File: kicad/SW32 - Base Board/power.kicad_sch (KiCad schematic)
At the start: 35 parts, among them J23 PWR, J24 BAT, SW1 PWR, U5 LM2941, U6 TPS5430DDA, U7 NCP1117LP

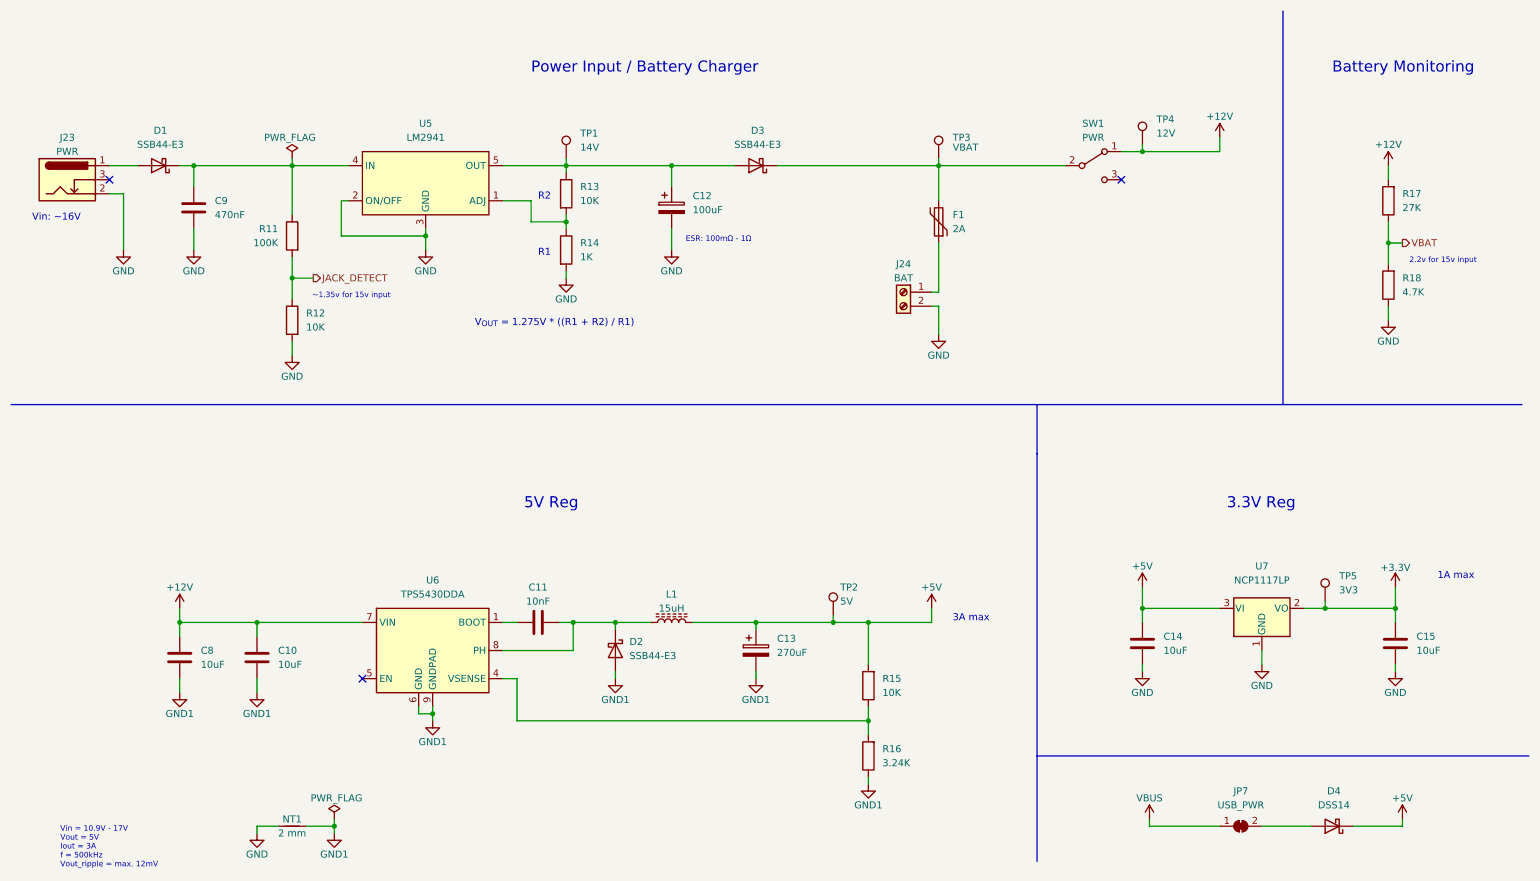
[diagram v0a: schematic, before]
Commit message: use ESP32
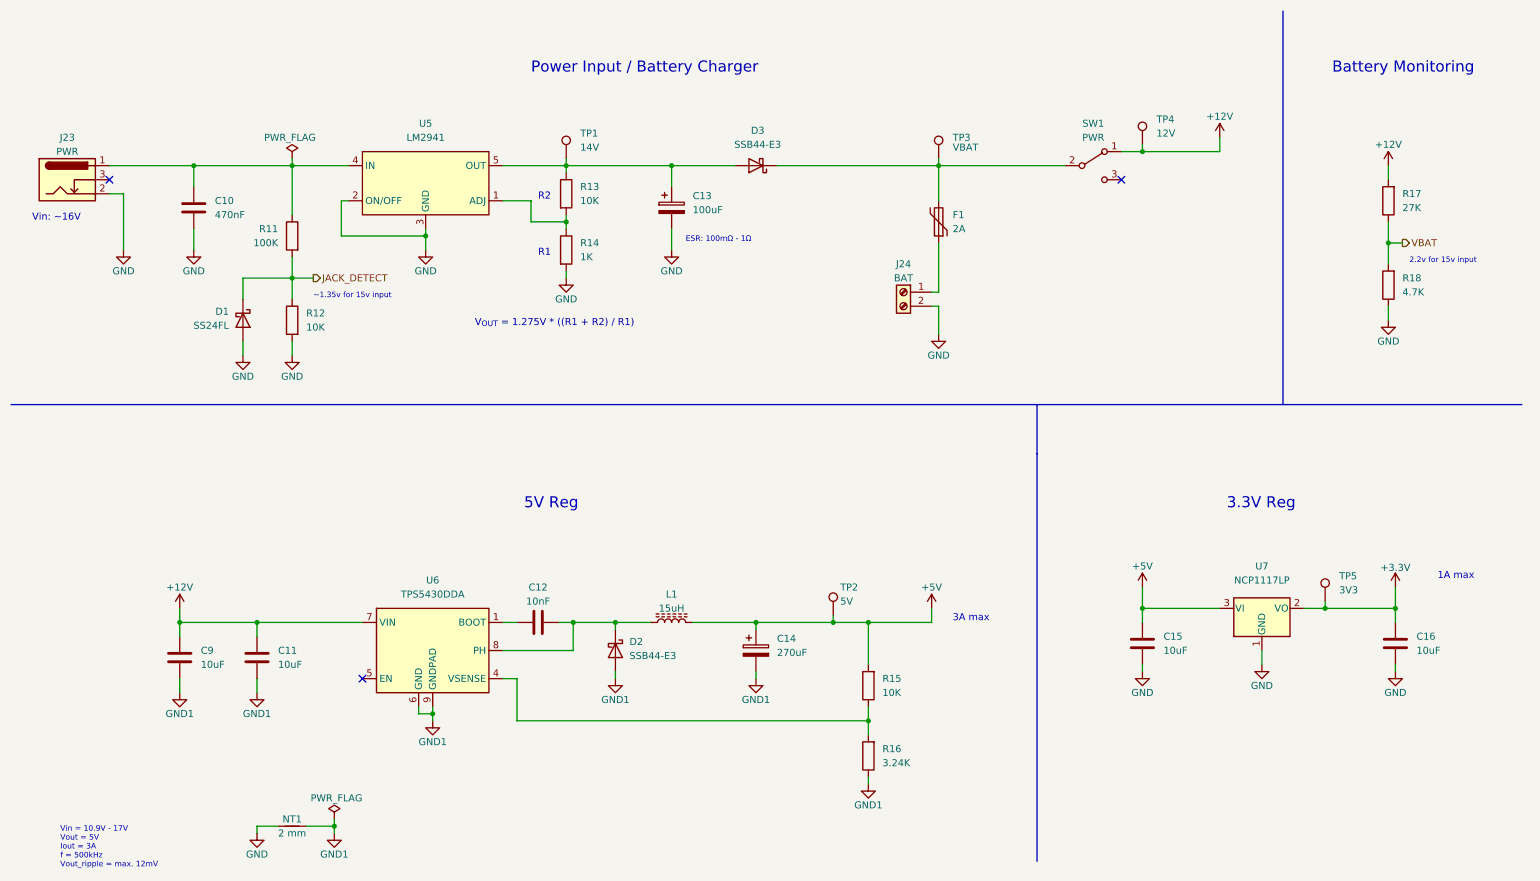
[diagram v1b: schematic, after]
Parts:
- removed D4: DSS14, Diode_SMD:D_SOD-123F, symbol Device:D_Schottky
- removed JP7: USB_PWR, Jumper:SolderJumper-2_P1.3mm_Bridged_RoundedPad1.0x1.5mm, symbol Jumper:SolderJumper_2_Bridged
- D1: value SSB44-E3 -> SS24FL; footprint Diode_SMD:D_SMB -> Diode_SMD:D_SOD-123F; LCSC C466999 -> C894433; MOUSER 625-SSB44-E3 -> 512-SS24FL; MPN SSB44-E3/52T -> SS24FL
- renumbered C9 to C10, C10 to C11, C11 to C12, C12 to C13, C13 to C14, C14 to C15, C15 to C16, C8 to C9
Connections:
- net GND: now also D1.2 (A)
- net JACK_DETECT: now also D1.1 (K)
- net at C10.1, R11.1, U5.4 (IN): now also J23.1; no longer D1.1 (K)
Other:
- moved on the sheet: D1

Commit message: add cap
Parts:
- renumbered C9 to C10, C10 to C11, C11 to C12, C12 to C13, C13 to C14, C14 to C15, C15 to C16, C16 to C17
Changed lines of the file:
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@@
   (symbol (lib_id "Device:C") (at 215.9 127 0) (unit 1)
     (in_bom yes) (on_board yes) (fields_autoplaced)
-    (property "Reference" "C15" (id 0) (at 219.71 125.7299 0)
+    (property "Reference" "C16" (id 0) (at 219.71 125.7299 0)
       (effects (font (size 1.27 1.27)) (justify left))
     )
@@
   (symbol (lib_id "power:GND1") (at 87.63 140.97 0) (unit 1)
     (in_bom yes) (on_board yes)
-    (property "Reference" "#PWR068" (id 0) (at 87.63 147.32 0)
+    (property "Reference" "#PWR070" (id 0) (at 87.63 147.32 0)
       (effects (font (size 1.27 1.27)) hide)
     )
@@
   (symbol (lib_id "power:GND") (at 53.34 74.93 0) (mirror y) (unit 1)
     (in_bom yes) (on_board yes)
-    (property "Reference" "#PWR062" (id 0) (at 53.34 81.28 0)
+    (property "Reference" "#PWR064" (id 0) (at 53.34 81.28 0)
       (effects (font (size 1.27 1.27)) hide)
     )
@@
   (symbol (lib_id "power:+12V") (at 41.91 120.65 0) (unit 1)
     (in_bom yes) (on_board yes)
-    (property "Reference" "#PWR059" (id 0) (at 41.91 124.46 0)
+    (property "Reference" "#PWR061" (id 0) (at 41.91 124.46 0)
       (effects (font (size 1.27 1.27)) hide)
     )
@@
   (symbol (lib_id "power:GND") (at 86.36 55.88 0) (unit 1)
     (in_bom yes) (on_board yes)
-    (property "Reference" "#PWR067" (id 0) (at 86.36 62.23 0)
+    (property "Reference" "#PWR069" (id 0) (at 86.36 62.23 0)
       (effects (font (size 1.27 1.27)) hide)
     )
@@
   (symbol (lib_id "Device:C") (at 106.68 123.19 90) (unit 1)
     (in_bom yes) (on_board yes)
-    (property "Reference" "C12" (id 0) (at 106.68 116.84 90))
+    (property "Reference" "C13" (id 0) (at 106.68 116.84 90))
     (property "Value" "10nF" (id 1) (at 106.68 119.38 90))
     (property "Footprint" "Capacitor_SMD:C_0603_1608Metric" (id 2) (at 110.49 122.2248 0)
@@
   (symbol (lib_id "power:+12V") (at 229.87 35.56 0) (unit 1)
     (in_bom yes) (on_board yes)
-    (property "Reference" "#PWR078" (id 0) (at 229.87 39.37 0)
+    (property "Reference" "#PWR080" (id 0) (at 229.87 39.37 0)
       (effects (font (size 1.27 1.27)) hide)
     )
@@
   (symbol (lib_id "power:GND") (at 111.76 60.96 0) (unit 1)
     (in_bom yes) (on_board yes)
-    (property "Reference" "#PWR069" (id 0) (at 111.76 67.31 0)
+    (property "Reference" "#PWR071" (id 0) (at 111.76 67.31 0)
       (effects (font (size 1.27 1.27)) hide)
     )
@@
   (symbol (lib_id "power:GND") (at 260.35 68.58 0) (unit 1)
     (in_bom yes) (on_board yes)
-    (property "Reference" "#PWR081" (id 0) (at 260.35 74.93 0)
+    (property "Reference" "#PWR083" (id 0) (at 260.35 74.93 0)
       (effects (font (size 1.27 1.27)) hide)
     )
@@
   (symbol (lib_id "power:GND") (at 62.23 74.93 0) (mirror y) (unit 1)
     (in_bom yes) (on_board yes)
-    (property "Reference" "#PWR065" (id 0) (at 62.23 81.28 0)
+    (property "Reference" "#PWR067" (id 0) (at 62.23 81.28 0)
       (effects (font (size 1.27 1.27)) hide)
     )
@@
   (symbol (lib_id "power:+5V") (at 215.9 116.84 0) (unit 1)
     (in_bom yes) (on_board yes)
-    (property "Reference" "#PWR076" (id 0) (at 215.9 120.65 0)
+    (property "Reference" "#PWR078" (id 0) (at 215.9 120.65 0)
       (effects (font (size 1.27 1.27)) hide)
     )
@@
   (symbol (lib_id "power:GND1") (at 69.85 161.29 0) (mirror y) (unit 1)
     (in_bom yes) (on_board yes)
-    (property "Reference" "#PWR066" (id 0) (at 69.85 167.64 0)
+    (property "Reference" "#PWR068" (id 0) (at 69.85 167.64 0)
       (effects (font (size 1.27 1.27)) hide)
     )
@@
   (symbol (lib_id "power:GND") (at 44.45 55.88 0) (unit 1)
     (in_bom yes) (on_board yes)
-    (property "Reference" "#PWR061" (id 0) (at 44.45 62.23 0)
+    (property "Reference" "#PWR063" (id 0) (at 44.45 62.23 0)
       (effects (font (size 1.27 1.27)) hide)
     )
@@
   (symbol (lib_id "power:GND") (at 130.81 55.88 0) (unit 1)
     (in_bom yes) (on_board yes)
-    (property "Reference" "#PWR071" (id 0) (at 130.81 62.23 0)
+    (property "Reference" "#PWR073" (id 0) (at 130.81 62.23 0)
       (effects (font (size 1.27 1.27)) hide)
     )
@@
   (symbol (lib_id "power:GND") (at 179.07 71.12 0) (unit 1)
     (in_bom yes) (on_board yes)
-    (property "Reference" "#PWR075" (id 0) (at 179.07 77.47 0)
+    (property "Reference" "#PWR077" (id 0) (at 179.07 77.47 0)
       (effects (font (size 1.27 1.27)) hide)
     )
@@
   (symbol (lib_id "Device:C") (at 44.45 48.26 0) (unit 1)
     (in_bom yes) (on_board yes) (fields_autoplaced)
-    (property "Reference" "C10" (id 0) (at 48.26 46.9899 0)
+    (property "Reference" "C11" (id 0) (at 48.26 46.9899 0)
       (effects (font (size 1.27 1.27)) (justify left))
     )
@@
   (symbol (lib_id "Device:C_Polarized") (at 146.05 128.27 0) (unit 1)
     (in_bom yes) (on_board yes) (fields_autoplaced)
-    (property "Reference" "C14" (id 0) (at 149.86 126.1109 0)
+    (property "Reference" "C15" (id 0) (at 149.86 126.1109 0)
       (effects (font (size 1.27 1.27)) (justify left))
     )
@@
   (symbol (lib_id "power:GND") (at 55.88 161.29 0) (unit 1)
     (in_bom yes) (on_board yes)
-    (property "Reference" "#PWR064" (id 0) (at 55.88 167.64 0)
+    (property "Reference" "#PWR066" (id 0) (at 55.88 167.64 0)
       (effects (font (size 1.27 1.27)) hide)
     )
@@
   (symbol (lib_id "power:GND1") (at 55.88 135.89 0) (unit 1)
     (in_bom yes) (on_board yes)
-    (property "Reference" "#PWR063" (id 0) (at 55.88 142.24 0)
+    (property "Reference" "#PWR065" (id 0) (at 55.88 142.24 0)
       (effects (font (size 1.27 1.27)) hide)
     )
@@
   (symbol (lib_id "Device:C_Polarized") (at 130.81 48.26 0) (unit 1)
     (in_bom yes) (on_board yes) (fields_autoplaced)
-    (property "Reference" "C13" (id 0) (at 134.62 46.1009 0)
+    (property "Reference" "C14" (id 0) (at 134.62 46.1009 0)
       (effects (font (size 1.27 1.27)) (justify left))
     )
@@
   (symbol (lib_id "power:GND1") (at 166.37 152.4 0) (unit 1)
     (in_bom yes) (on_board yes)
-    (property "Reference" "#PWR073" (id 0) (at 166.37 158.75 0)
+    (property "Reference" "#PWR075" (id 0) (at 166.37 158.75 0)
       (effects (font (size 1.27 1.27)) hide)
     )
@@
   (symbol (lib_id "Device:C") (at 55.88 129.54 180) (unit 1)
     (in_bom yes) (on_board yes) (fields_autoplaced)
-    (property "Reference" "C11" (id 0) (at 59.69 128.2699 0)
+    (property "Reference" "C12" (id 0) (at 59.69 128.2699 0)
       (effects (font (size 1.27 1.27)) (justify right))
     )
@@
   (symbol (lib_id "power:GND") (at 31.75 55.88 0) (unit 1)
     (in_bom yes) (on_board yes)
-    (property "Reference" "#PWR058" (id 0) (at 31.75 62.23 0)
+    (property "Reference" "#PWR060" (id 0) (at 31.75 62.23 0)
       (effects (font (size 1.27 1.27)) hide)
     )
@@
   (symbol (lib_id "power:+3.3V") (at 261.62 116.84 0) (unit 1)
     (in_bom yes) (on_board yes)
-    (property "Reference" "#PWR082" (id 0) (at 261.62 120.65 0)
+    (property "Reference" "#PWR084" (id 0) (at 261.62 120.65 0)
       (effects (font (size 1.27 1.27)) hide)
     )
@@
   (symbol (lib_id "power:+5V") (at 177.8 120.65 0) (unit 1)
     (in_bom yes) (on_board yes)
-    (property "Reference" "#PWR074" (id 0) (at 177.8 124.46 0)
+    (property "Reference" "#PWR076" (id 0) (at 177.8 124.46 0)
       (effects (font (size 1.27 1.27)) hide)
     )
@@
   (symbol (lib_id "power:GND") (at 261.62 132.08 0) (mirror y) (unit 1)
     (in_bom yes) (on_board yes)
-    (property "Reference" "#PWR083" (id 0) (at 261.62 138.43 0)
+    (property "Reference" "#PWR085" (id 0) (at 261.62 138.43 0)
       (effects (font (size 1.27 1.27)) hide)
     )
@@
   (symbol (lib_id "power:GND1") (at 146.05 133.35 0) (unit 1)
     (in_bom yes) (on_board yes)
-    (property "Reference" "#PWR072" (id 0) (at 146.05 139.7 0)
+    (property "Reference" "#PWR074" (id 0) (at 146.05 139.7 0)
       (effects (font (size 1.27 1.27)) hide)
     )
@@
   (symbol (lib_id "power:GND") (at 215.9 132.08 0) (mirror y) (unit 1)
     (in_bom yes) (on_board yes)
-    (property "Reference" "#PWR077" (id 0) (at 215.9 138.43 0)
+    (property "Reference" "#PWR079" (id 0) (at 215.9 138.43 0)
       (effects (font (size 1.27 1.27)) hide)
     )
@@
   (symbol (lib_id "Device:C") (at 261.62 127 0) (unit 1)
     (in_bom yes) (on_board yes) (fields_autoplaced)
-    (property "Reference" "C16" (id 0) (at 265.43 125.7299 0)
+    (property "Reference" "C17" (id 0) (at 265.43 125.7299 0)
       (effects (font (size 1.27 1.27)) (justify left))
     )
@@
   (symbol (lib_id "Device:C") (at 41.91 129.54 180) (unit 1)
     (in_bom yes) (on_board yes) (fields_autoplaced)
-    (property "Reference" "C9" (id 0) (at 45.72 128.2699 0)
+    (property "Reference" "C10" (id 0) (at 45.72 128.2699 0)
       (effects (font (size 1.27 1.27)) (justify right))
     )
@@
   (symbol (lib_id "power:+12V") (at 260.35 40.64 0) (unit 1)
     (in_bom yes) (on_board yes)
-    (property "Reference" "#PWR080" (id 0) (at 260.35 44.45 0)
+    (property "Reference" "#PWR082" (id 0) (at 260.35 44.45 0)
       (effects (font (size 1.27 1.27)) hide)
     )
@@
   (symbol (lib_id "power:GND1") (at 41.91 135.89 0) (unit 1)
     (in_bom yes) (on_board yes)
-    (property "Reference" "#PWR060" (id 0) (at 41.91 142.24 0)
+    (property "Reference" "#PWR062" (id 0) (at 41.91 142.24 0)
       (effects (font (size 1.27 1.27)) hide)
     )
@@
   (symbol (lib_id "power:GND1") (at 120.65 133.35 0) (unit 1)
     (in_bom yes) (on_board yes)
-    (property "Reference" "#PWR070" (id 0) (at 120.65 139.7 0)
+    (property "Reference" "#PWR072" (id 0) (at 120.65 139.7 0)
       (effects (font (size 1.27 1.27)) hide)
     )
@@
   (symbol (lib_id "power:GND") (at 237.49 130.81 0) (mirror y) (unit 1)
     (in_bom yes) (on_board yes)
-    (property "Reference" "#PWR079" (id 0) (at 237.49 137.16 0)
-      (effects (font (size 1.27 1.27)) hide)
-    )
+    (property "Reference" "#PWR081" (id 0) (at 237.49 137.16 0)
+      (effects (font (size 1.27 1.27)) hide)
+    )

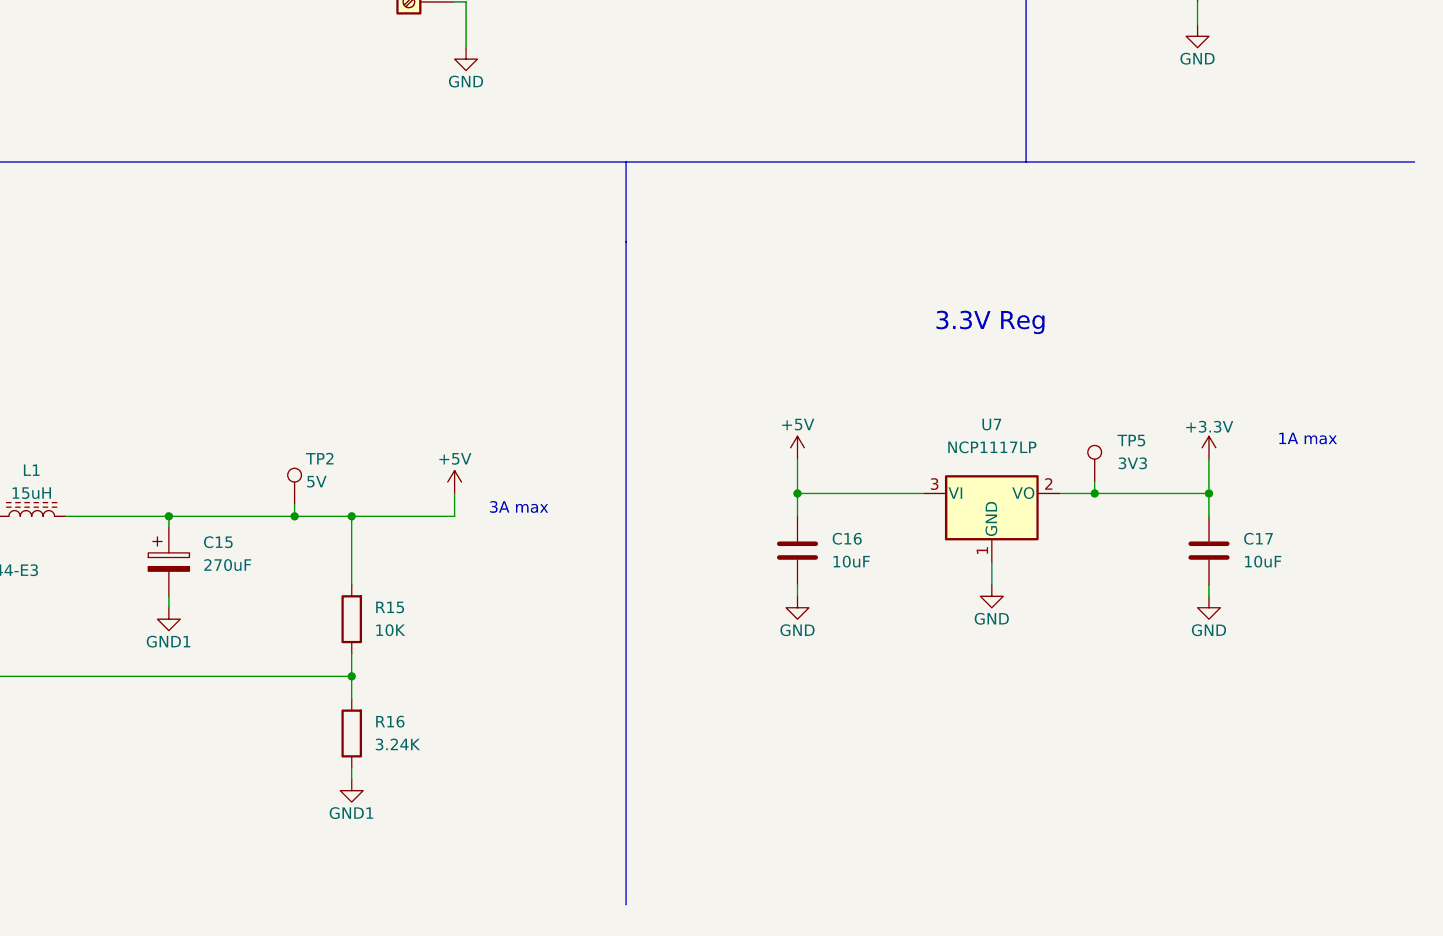
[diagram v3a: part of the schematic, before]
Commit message: add power led
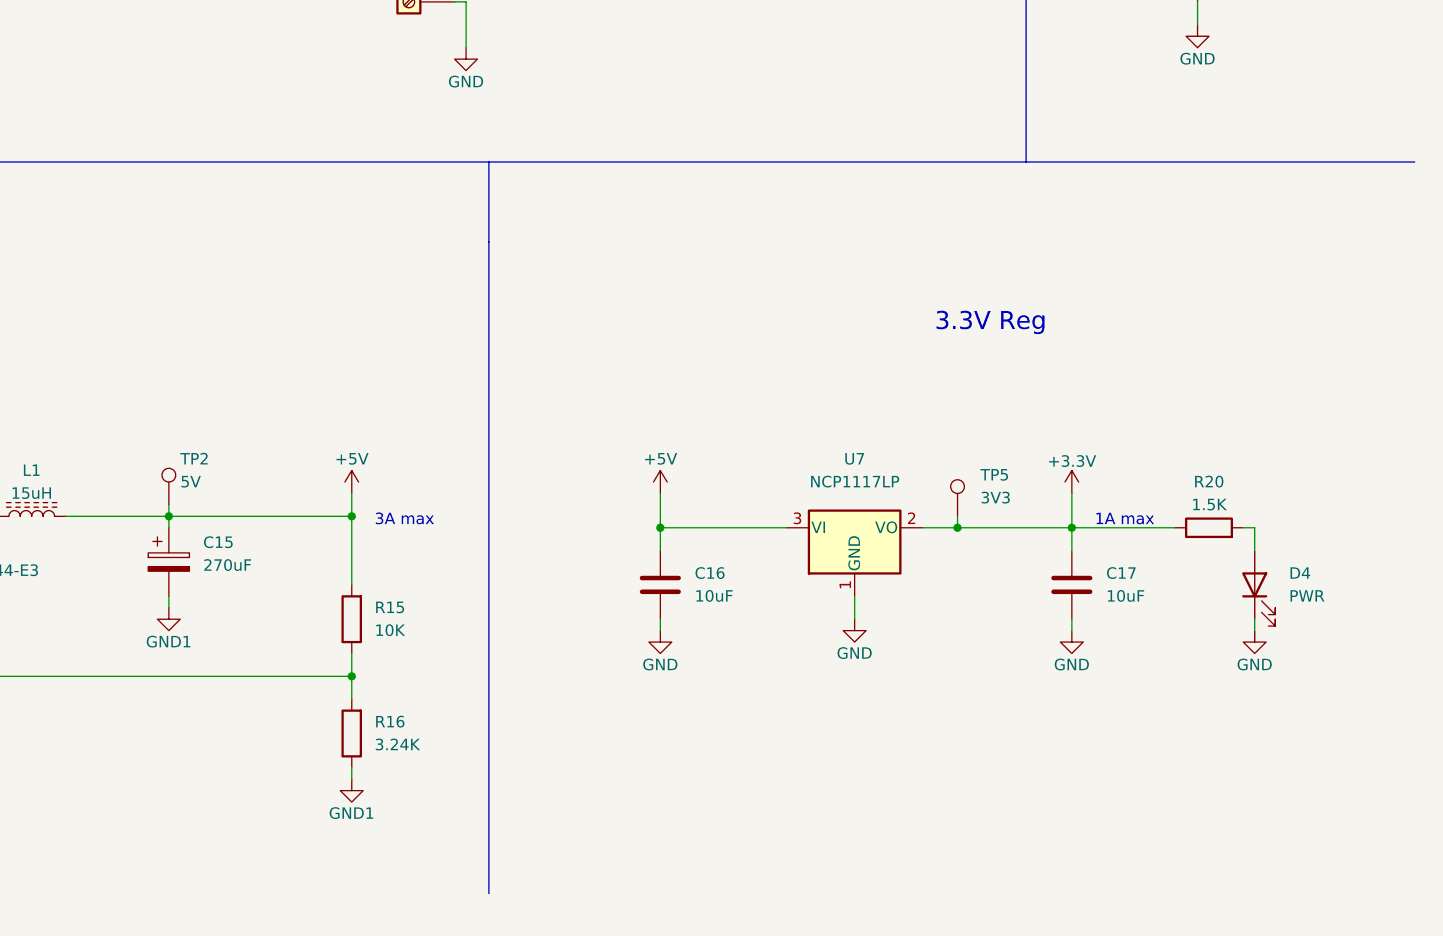
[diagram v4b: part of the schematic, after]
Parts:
- added D4: PWR, LED_SMD:LED_0603_1608Metric, symbol Device:LED
- added R20: 1.5K, Resistor_SMD:R_0603_1608Metric, symbol Device:R
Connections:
- net +3.3V: now also R20.1
- net GND: now also D4.1 (K)
- new net: D4.2 (A), R20.2
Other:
- moved on the sheet: C16, C17, TP2, TP5, U7
